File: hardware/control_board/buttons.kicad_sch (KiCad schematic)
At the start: 50 parts, among them IC2 74HC165, IC3 74HC165, IC8 74HC595, IC9 74HC165, SW1 Encoder

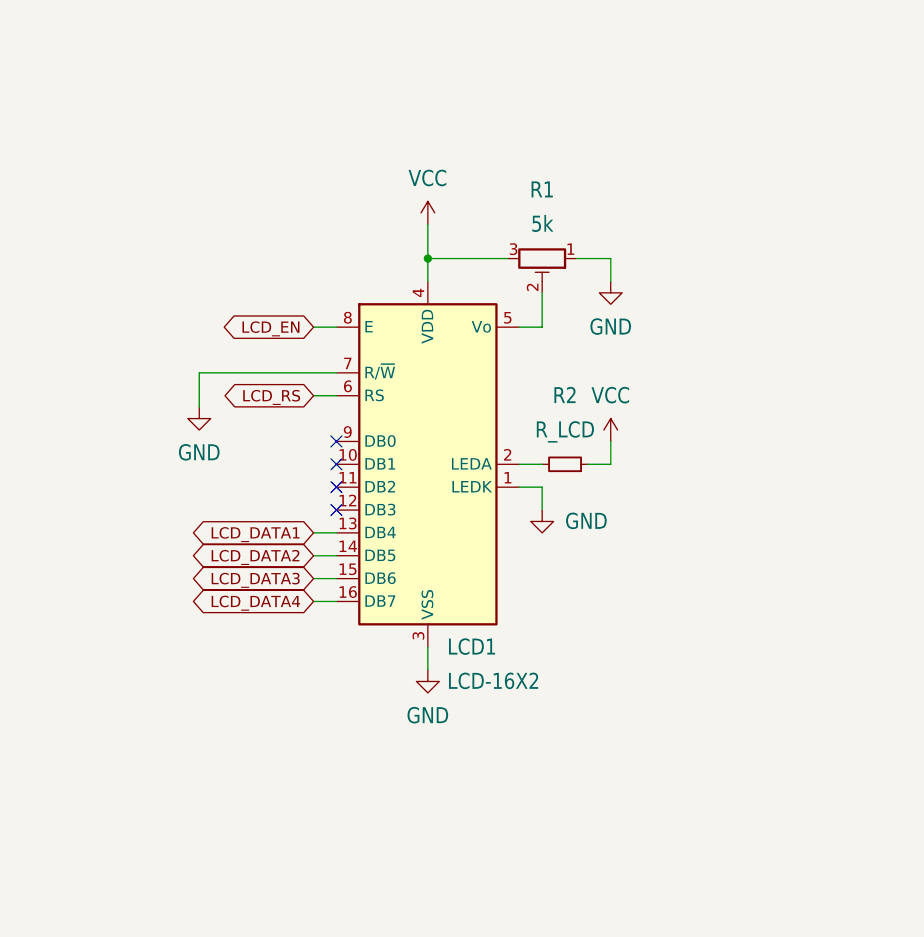
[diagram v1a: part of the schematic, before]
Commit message: update symbol and footprint for display
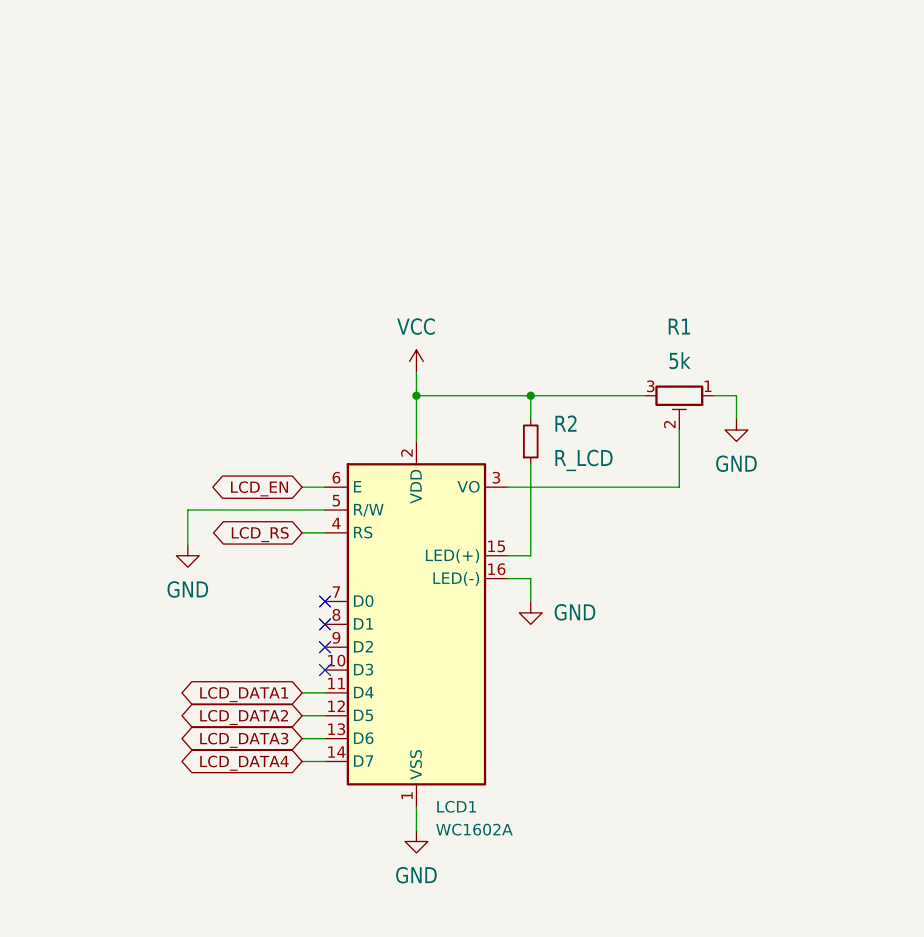
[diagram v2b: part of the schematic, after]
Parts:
- removed LCD1: LCD-16X2, shruthi_control_board_xt_v03:LCD-16X2, symbol Display_Character:HY1602E
- added LCD1: WC1602A, Display:WC1602A, symbol Display_Character:WC1602A
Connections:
- net GND: now also LCD1.1 (VSS), LCD1.16 (LED(-)), LCD1.5 (R/W)
- net LCD_DATA1: now also LCD1.11 (D4)
- net LCD_DATA2: now also LCD1.12 (D5)
- net LCD_DATA3: now also LCD1.13 (D6)
- net LCD_DATA4: now also LCD1.14 (D7)
- net LCD_EN: now also LCD1.6 (E)
- net LCD_RS: now also LCD1.4 (RS)
- net VCC: now also R2.2, LCD1.2 (VDD); no longer R2.1
- net at R1.2: now also LCD1.3 (VO)
- new net: LCD1.15 (LED(+)), R2.1
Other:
- moved on the sheet: R1, R2

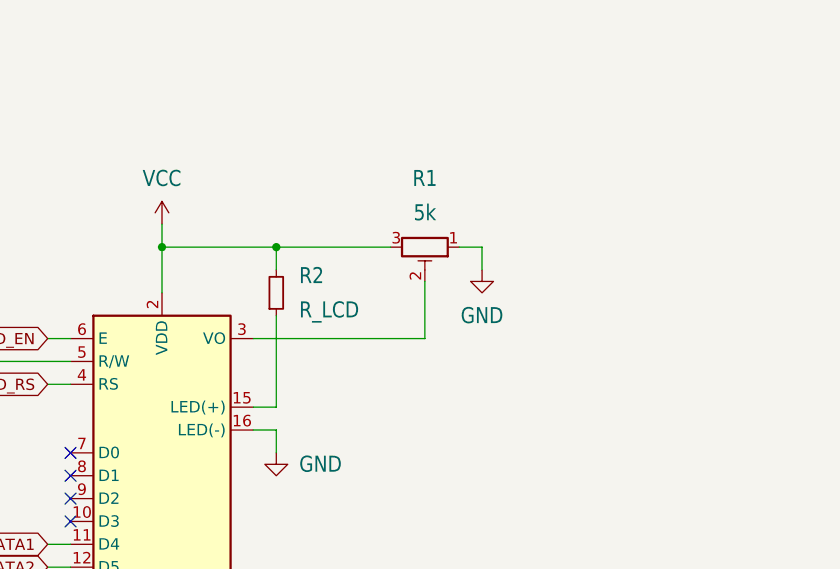
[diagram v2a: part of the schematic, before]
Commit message: update lcd LED and trimmer footprints
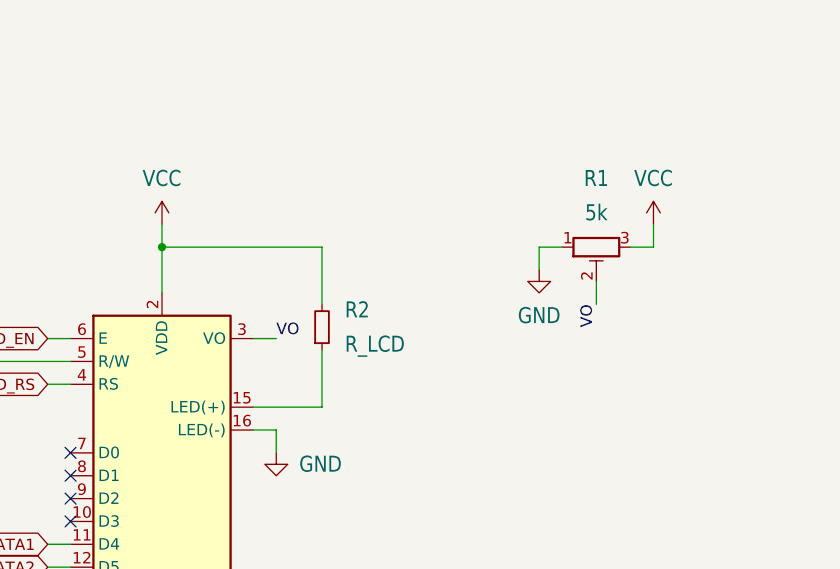
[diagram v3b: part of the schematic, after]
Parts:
- R1: footprint shruthi_control_board_xt_v03:RTRIM3339P -> Potentiometer_THT:Potentiometer_Bourns_3296W_Vertical
- R2: footprint shruthi_control_board_xt_v03:0204_7 -> Resistor_THT:R_Axial_DIN0204_L3.6mm_D1.6mm_P7.62mm_Horizontal
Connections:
- net VO: now reaches LCD1.3 (VO), R1.2
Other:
- moved on the sheet: R1, R2
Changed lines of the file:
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@@
 	)
 	(junction
-		(at 195.58 212.09)
-		(diameter 0)
-		(color 0 0 0 0)
-	)
-	(junction
 		(at 370.84 175.26)
 		(diameter 0)
@@
 	(wire
 		(pts
+			(xy 237.49 212.09) (xy 234.95 212.09)
+		)
+		(stroke
+			(width 0)
+			(type default)
+		)
+	)
+	(wire
+		(pts
 			(xy 355.6 132.08) (xy 358.14 132.08)
 		)
@@
 	(wire
 		(pts
+			(xy 224.79 212.09) (xy 224.79 214.63)
+		)
+		(stroke
+			(width 0)
+			(type default)
+		)
+	)
+	(wire
+		(pts
 			(xy 279.4 132.08) (xy 279.4 129.54)
 		)
@@
 	(wire
 		(pts
-			(xy 212.09 215.9) (xy 212.09 222.25)
+			(xy 231.14 215.9) (xy 231.14 218.44)
 		)
 		(stroke
@@
 	(wire
 		(pts
+			(xy 193.04 222.25) (xy 195.58 222.25)
+		)
+		(stroke
+			(width 0)
+			(type default)
+		)
+	)
+	(wire
+		(pts
 			(xy 350.52 99.06) (xy 350.52 149.86)
 		)
@@
 	(wire
 		(pts
+			(xy 237.49 209.55) (xy 237.49 212.09)
+		)
+		(stroke
+			(width 0)
+			(type default)
+		)
+	)
+	(wire
+		(pts
 			(xy 88.9 66.04) (xy 93.98 66.04)
 		)
@@
 	(wire
 		(pts
-			(xy 195.58 219.71) (xy 195.58 229.87)
+			(xy 200.66 223.52) (xy 200.66 229.87)
 		)
 		(stroke
@@
 	(wire
 		(pts
-			(xy 195.58 212.09) (xy 208.28 212.09)
+			(xy 34.29 193.04) (xy 34.29 190.5)
 		)
 		(stroke
@@
 	(wire
 		(pts
-			(xy 34.29 193.04) (xy 34.29 190.5)
+			(xy 93.98 53.34) (xy 93.98 66.04)
 		)
 		(stroke
-			(width 0)
-			(type default)
+			(width 0.1524)
+			(type solid)
 		)
 	)
 	(wire
 		(pts
-			(xy 93.98 53.34) (xy 93.98 66.04)
+			(xy 227.33 212.09) (xy 224.79 212.09)
 		)
 		(stroke
-			(width 0.1524)
-			(type solid)
+			(width 0)
+			(type default)
 		)
 	)
@@
 	(wire
 		(pts
-			(xy 195.58 229.87) (xy 193.04 229.87)
+			(xy 200.66 229.87) (xy 193.04 229.87)
 		)
 		(stroke
@@
 	(wire
 		(pts
-			(xy 182.88 212.09) (xy 195.58 212.09)
+			(xy 182.88 212.09) (xy 200.66 212.09)
 		)
 		(stroke
@@
 	(wire
 		(pts
-			(xy 195.58 212.09) (xy 195.58 214.63)
+			(xy 200.66 212.09) (xy 200.66 218.44)
 		)
 		(stroke
@@
 	(wire
 		(pts
-			(xy 218.44 212.09) (xy 218.44 214.63)
-		)
-		(stroke
-			(width 0)
-			(type default)
-		)
-	)
-	(wire
-		(pts
 			(xy 24.13 101.6) (xy 24.13 106.68)
 		)
@@
 	(wire
 		(pts
-			(xy 215.9 212.09) (xy 218.44 212.09)
-		)
-		(stroke
-			(width 0)
-			(type default)
-		)
-	)
-	(wire
-		(pts
 			(xy 237.49 114.3) (xy 242.57 114.3)
 		)
@@
 	(wire
 		(pts
-			(xy 193.04 222.25) (xy 212.09 222.25)
-		)
-		(stroke
-			(width 0)
-			(type default)
-		)
-	)
-	(wire
-		(pts
 			(xy 154.94 111.76) (xy 152.4 111.76)
 		)
@@
 		)
 	)
+	(label "VO"
+		(at 195.58 222.25 0)
+		(effects
+			(font
+				(size 1.27 1.27)
+			)
+			(justify left bottom)
+		)
+	)
+	(label "VO"
+		(at 231.14 218.44 270)
+		(effects
+			(font
+				(size 1.27 1.27)
+			)
+			(justify right bottom)
+		)
+	)
 	(label "INPUT_CHAIN_2"
 		(at 355.6 124.46 90)
@@
 	(symbol
 		(lib_id "Device:R_Small")
-		(at 195.58 217.17 0)
+		(at 200.66 220.98 0)
 		(mirror x)
 		(unit 1)
@@
 		(fields_autoplaced yes)
 		(property "Reference" "R2"
-			(at 198.12 215.265 0)
+			(at 203.2 219.075 0)
 			(effects
 				(font
@@
 		)
 		(property "Value" "R_LCD"
-			(at 198.12 219.075 0)
+			(at 203.2 222.885 0)
 			(effects
 				(font
@@
 			)
 		)
-		(property "Footprint" "shruthi_control_board_xt_v03:0204_7"
-			(at 195.58 217.17 0)
+		(property "Footprint" "Resistor_THT:R_Axial_DIN0204_L3.6mm_D1.6mm_P7.62mm_Horizontal"
+			(at 200.66 220.98 0)
 			(effects
 				(font
@@
 		)
 		(property "Datasheet" "~"
-			(at 195.58 217.17 0)
+			(at 200.66 220.98 0)
 			(effects
 				(font
@@
 		)
 		(property "Description" "Resistor, small symbol"
-			(at 195.58 217.17 0)
+			(at 200.66 220.98 0)
 			(effects
 				(font
@@
 	(symbol
 		(lib_id "Device:R_Potentiometer_Trim")
-		(at 212.09 212.09 270)
+		(at 231.14 212.09 90)
+		(mirror x)
 		(unit 1)
 		(exclude_from_sim no)
@@
 		(fields_autoplaced yes)
 		(property "Reference" "R1"
-			(at 212.09 204.47 90)
+			(at 231.14 204.47 90)
 			(effects
 				(font
@@
 		)
 		(property "Value" "5k"
-			(at 212.09 208.28 90)
+			(at 231.14 208.28 90)
 			(effects
 				(font
@@
 			)
 		)
-		(property "Footprint" "shruthi_control_board_xt_v03:RTRIM3339P"
-			(at 212.09 212.09 0)
+		(property "Footprint" "Potentiometer_THT:Potentiometer_Bourns_3296W_Vertical"
+			(at 231.14 212.09 0)
 			(effects
 				(font
@@
 		)
 		(property "Datasheet" "~"
-			(at 212.09 212.09 0)
+			(at 231.14 212.09 0)
 			(effects
 				(font
@@
 		)
 		(property "Description" "Trim-potentiometer"
-			(at 212.09 212.09 0)
+			(at 231.14 212.09 0)
 			(effects
 				(font
@@
 	(symbol
 		(lib_id "power:GND")
-		(at 218.44 214.63 0)
+		(at 224.79 214.63 0)
+		(mirror y)
 		(unit 1)
 		(exclude_from_sim no)
@@
 		(fields_autoplaced yes)
 		(property "Reference" "#GND015"
-			(at 218.44 214.63 0)
+			(at 224.79 214.63 0)
 			(effects
 				(font
@@
 		)
 		(property "Value" "GND"
-			(at 218.44 219.71 0)
+			(at 224.79 219.71 0)
 			(effects
 				(font
@@
 		)
 		(property "Footprint" ""
-			(at 218.44 214.63 0)
+			(at 224.79 214.63 0)
 			(effects
 				(font
@@
 		)
 		(property "Datasheet" ""
-			(at 218.44 214.63 0)
+			(at 224.79 214.63 0)
 			(effects
 				(font
@@
 		)
 		(property "Description" "Power symbol creates a global label with name \"GND\" , ground"
-			(at 218.44 214.63 0)
+			(at 224.79 214.63 0)
 			(effects
 				(font
@@
 					(unit 1)
 				)
+			)
+		)
+	)
+	(symbol
+		(lib_id "power:VCC")
+		(at 237.49 209.55 0)
+		(unit 1)
+		(exclude_from_sim no)
+		(in_bom yes)
+		(on_board yes)
+		(dnp no)
+		(fields_autoplaced yes)
+		(property "Reference" "#P+016"
+			(at 237.49 209.55 0)
+			(effects
+				(font
+					(size 1.27 1.27)
+				)
+				(hide yes)
+			)
+		)
+		(property "Value" "VCC"
+			(at 237.49 204.47 0)
+			(effects
+				(font
+					(size 1.778 1.5113)
+				)
+			)
+		)
+		(property "Footprint" ""
+			(at 237.49 209.55 0)
+			(effects
+				(font
+					(size 1.27 1.27)
+				)
+				(hide yes)
+			)
+		)
+		(property "Datasheet" ""
+			(at 237.49 209.55 0)
+			(effects
+				(font
+					(size 1.27 1.27)
+				)
+				(hide yes)
+			)
+		)
+		(property "Description" "Power symbol creates a global label with name \"VCC\""
+			(at 237.49 209.55 0)
+			(effects
+				(font
+					(size 1.27 1.27)
+				)
+				(hide yes)
+			)
+		)
+		(pin "1"
+		)
+		(instances
+			(project "control_board"
+				(path "/2c840835-6e01-4901-947c-222cae369ab9/1e4cf160-db0f-4db8-aa2b-cf7d135880af"
+					(reference "#P+016")
+					(unit 1)
+				)

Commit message: move all logic components to daughterboard, move MIDI to new board
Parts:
- removed C13, C14, C2, C3: 100n, shruthi_control_board_xt_v03:C025-024X044, symbol Device:C_Small
- removed IC2, IC3, IC9: 74HC165, Package_DIP:DIP-16_W7.62mm_Socket_LongPads, symbol 74xx:74HC165
- removed IC8: 74HC595, Package_DIP:DIP-16_W7.62mm_Socket_LongPads, symbol 74xx:74HC595
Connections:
- no-connect marks 12 -> 9
